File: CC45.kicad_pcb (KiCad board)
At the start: 2 copper layers, 247 x 80.8 mm, 123 parts, among them SW1 RESET, SW10 K08, SW11 K09, SW12 K0A, SW13 K0B, SW14 K0C, SW15 K10, SW16 K11, SW17 K12, SW18 K13, SW19 K14, SW2 K00, SW20 K15, SW21 K16, SW22 K17, SW23 K18, SW24 K19, SW25 K1A, SW26 K1B, SW27 K20, SW28 K21, SW29 K22, SW3 K01, SW30 K23, SW31 K24, SW32 K25, SW33 K26, SW34 K27, SW35 K28, SW36 K29, SW37 K2A, SW38 K2B, SW39 K30, SW4 K02, SW40 K31, SW41 K32, SW42 K33, SW43 K34, SW44 K36, SW45 K38, SW46 K39, SW47 K3A, SW48 K3B, SW5 K03, SW6 K04, SW7 K05, SW8 K06, SW9 K07, U1 ATmega32U4-AU, U2 PRTR5V0U2X, X1 XTAL

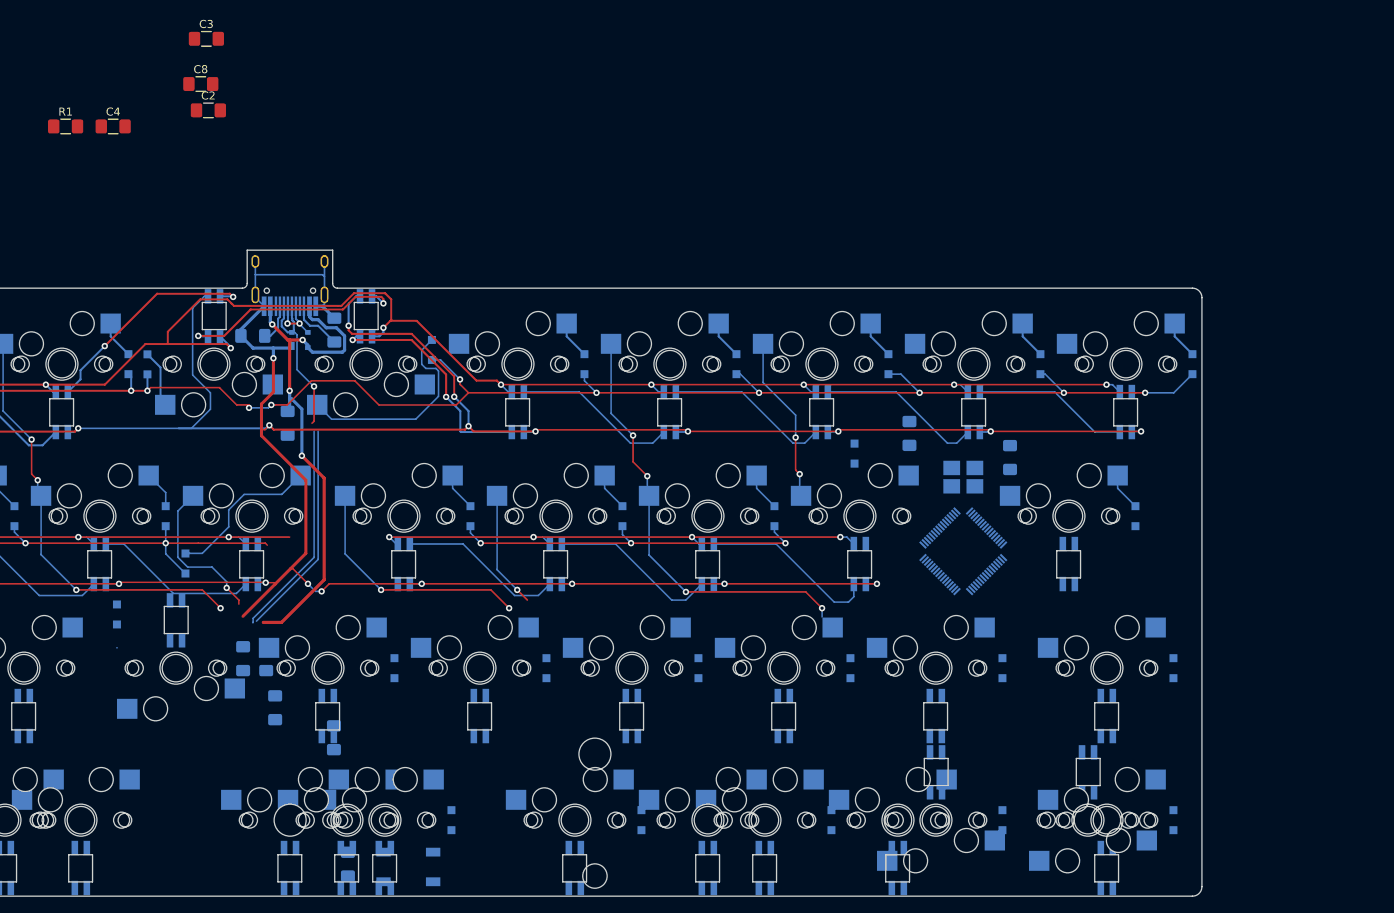
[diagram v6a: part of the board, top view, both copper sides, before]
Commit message: switch to 0805
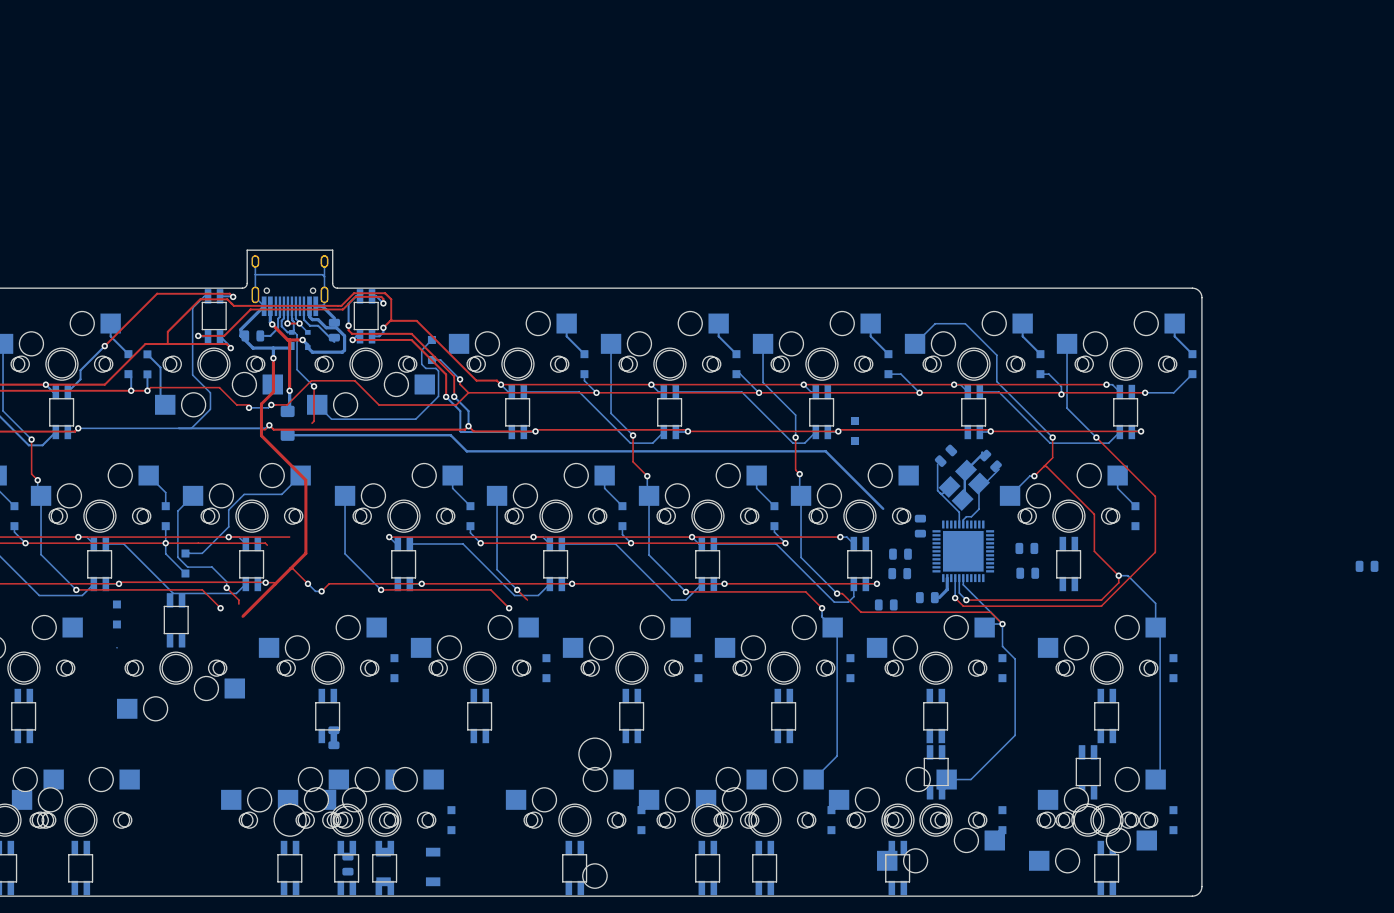
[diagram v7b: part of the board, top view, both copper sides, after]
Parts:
- C1, C5, C6, C7: footprint Capacitor_SMD:C_1206_3216Metric_Pad1.42x1.75mm_HandSolder -> Capacitor_SMD:C_0805_2012Metric
- C2, C3, C4, C8: footprint Capacitor_SMD:C_1206_3216Metric_Pad1.42x1.75mm_HandSolder -> Capacitor_SMD:C_0805_2012Metric; moved to B.Cu
- R1: footprint Resistor_SMD:R_1206_3216Metric_Pad1.42x1.75mm_HandSolder -> Resistor_SMD:R_0805_2012Metric; moved to B.Cu
- R2, R3, R4, R5, R6: footprint Resistor_SMD:R_1206_3216Metric_Pad1.42x1.75mm_HandSolder -> Resistor_SMD:R_0805_2012Metric
- U1: footprint Package_QFP:TQFP-64_7x7mm_P0.4mm -> libs:QFN44G-0.5-7X7MM
- moved R1 171.7 mm to (291.4, 58.5), turned to 180 degrees
- moved C8 120.1 mm to (249.0, 59.4)
- moved C4 117.6 mm to (236.4, 62.4)
- moved C2 116.0 mm to (248.9, 56.3)
- moved C3 108.1 mm to (235.6, 53.5), turned to 90 degrees
- moved R2 82.8 mm to (233.0, 59.4), turned to 180 degrees
- moved R3 80.4 mm to (233.1, 57.0), turned to 180 degrees
- moved C5 77.5 mm to (231.3, 63.3), turned to 0 degrees
- moved C7 5.36 mm to (238.8, 44.7), turned to 45 degrees
- moved D24 2.83 mm to (227.4, 41.6)
- moved C6 2.45 mm to (244.3, 45.3), turned to 135 degrees
- moved X1 1.02 mm to (241.0, 48.4), turned to -135 degrees
- turned U1 to 0 degrees
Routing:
- net col11: track 0.00 -> 106.1 mm, vias 0 -> 4
- net Vcc: track 480.1 -> 558.4 mm
- net col10: track 21.0 -> 92.4 mm, vias 2 -> 4
- net col12: track 0.00 -> 61.4 mm, vias 0 -> 2
- net VCC: track 64.8 -> 30.4 mm, vias 4 -> 3
- net /USB_N: track 47.6 -> 20.5 mm
- net /USB_P: track 34.6 -> 7.66 mm
- net col9: track 53.8 -> 76.2 mm
- net Net-(SW12-Pad9): track 20.7 -> 0.00 mm
- net GND: track 577.6 -> 587.8 mm
- net XTAL2: track 0.00 -> 10.1 mm
- net XTAL1: track 0.00 -> 9.48 mm
- net Net-(SW13-Pad9): track 19.6 -> 20.7 mm
- net row0: track 273.8 -> 274.3 mm

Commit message: switch to 0603
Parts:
- C1, C2, C3, C4, C5, C6, C7, C8: footprint Capacitor_SMD:C_0805_2012Metric -> Capacitor_SMD:C_0603_1608Metric
- D1, D10, D11, D12, D13, D14, D15, D16, D17, D18, D19, D2, D20, D21, D22, D23, D24, D25, D26, D27, D28, D29, D3, D30, D31, D32, D33, D34, D35, D36, D37, D38, D39, D4, D40, D41, D42, D43, D44, D45, D46, D47, D5, D6, D7, D8, D9: footprint Diode_SMD:D_SOD-323_HandSoldering -> Diode_SMD:D_0603_1608Metric
- R1, R2, R3, R4, R5, R6: footprint Resistor_SMD:R_0805_2012Metric -> Resistor_SMD:R_0603_1608Metric
- X1: footprint Crystal:Crystal_SMD_3225-4Pin_3.2x2.5mm_HandSoldering -> Crystal:Crystal_SMD_2016-4Pin_2.0x1.6mm
- moved C5 8.54 mm to (232.9, 55.0), turned to -90 degrees
- moved C8 6.11 mm to (243.7, 62.5), turned to 180 degrees
- moved C7 3.59 mm to (239.2, 48.3)
- moved C6 3.30 mm to (242.7, 48.2)
- moved C3 2.78 mm to (237.1, 51.2), turned to 0 degrees
- moved C2 2.21 mm to (247.1, 55.0), turned to 90 degrees
- moved C4 1.63 mm to (238.0, 62.3)
- moved X1 1.45 mm to (240.9, 49.8)
- moved R2 1.06 mm to (233.7, 58.7)
- moved R3 0.64 mm to (233.7, 57.1)
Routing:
- net GND: track 587.8 -> 711.5 mm, vias 29 -> 36
- net col12: track 61.4 -> 0.00 mm, vias 2 -> 0
- net Vcc: track 558.4 -> 613.7 mm, vias 24 -> 27
- net col11: track 106.1 -> 82.1 mm, vias 4 -> 3
- net /USB_N: track 20.5 -> 7.68 mm, vias 1 -> 0
- net XTAL2: track 10.1 -> 1.87 mm
- net col10: track 92.4 -> 84.6 mm
- net XTAL1: track 9.48 -> 1.85 mm
- net D+: track 0.00 -> 3.32 mm
- net D-: track 0.00 -> 3.32 mm
- net VCC: track 30.4 -> 32.6 mm
- added copper zone on B.Cu, net GND
